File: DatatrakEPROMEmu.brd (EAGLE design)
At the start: 160 x 66 mm, 32 parts, among them IC1 LD1117AS33TR, IC2 XC95144XL_TQ144_P, U1 SN74LVCH16T245DGGR, U2 SN74LVCH16T245DGGR, U3 SN74LVCH16T245DGGR, U4 IS62WV25616DBLL-45TLI, U5 FT240XS, X1 MABC48B2, X2 PN61729-S

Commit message: first routable layout
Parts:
- added X3: (no value), con-molex:22-23-2061
- moved C9 35.3 mm to (119.4, 35.6), turned to 270 degrees
- moved C8 31.7 mm to (121.9, 35.6), turned to 270 degrees
- moved U5 23.3 mm to (128.3, 34.3), turned to 270 degrees
- moved R2 17.3 mm to (138.4, 27.9), turned to 180 degrees
- moved C7 15.3 mm to (143.5, 27.9), turned to 90 degrees
- moved R1 12.8 mm to (138.4, 31.8), turned to 180 degrees
- moved C19 10.3 mm to (48.3, 36.2)
- moved C20 10.3 mm to (67.3, 36.2)
- moved U4 10.3 mm to (57.8, 36.2)
- moved L1 9.25 mm to (138.4, 35.6), turned to 180 degrees
- moved C16 9.03 mm to (108.6, 33.0)
- moved C10 9.03 mm to (77.5, 46.4)
- moved C11 9.03 mm to (77.5, 41.3)
- moved C12 9.03 mm to (77.5, 31.1)
- moved C15 9.03 mm to (108.6, 25.4)
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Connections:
- removed net N$1: U3.1, U3.24
- new net /TGT_DEN: IC2.40, U3.25, U3.48
- new net A_LV18: IC2.53
- new net JTCK: IC2.67, X3.3
- new net JTDI: IC2.63, X3.1
- new net JTMS: IC2.65, X3.2
- new net TGT_DIR: IC2.41, U3.1, U3.24
- net +3V3: now also X3.5
- net /CE: now also U2.14; no longer U2.8
- net /CE_LV: now also IC2.43, U2.35; no longer U2.41
- net /OEH: now also U2.19; no longer U2.11
- net /OEH_LV: now also IC2.46, U2.30; no longer U2.38
- net /OEL: now also U2.17; no longer U2.9
- net /OEL_LV: now also IC2.45, U2.32; no longer U2.40
- net /PGMH: now also U1.20; no longer U2.6
- net /PGMH_LV: now also IC2.69, U1.29; no longer U2.43
- net /PGML: now also U1.23; no longer U2.5
- net /PGML_LV: now also IC2.71, U1.26; no longer U2.44
- net /RAM_CS: now also IC2.139
- net /RAM_LB: now also IC2.10
- net /RAM_OE: now also IC2.7
- net /RAM_UB: now also IC2.9
- net /RAM_WE: now also IC2.31
- net A0: now also U2.23; no longer U1.2
- net A1: now also U1.2; no longer U1.3
- net A10: now also U2.16; no longer U1.16
- net A11: now also U2.20; no longer U1.17
- net A12: now also U1.17; no longer U1.19
- net A13: now also U1.8; no longer U1.20
- net A14: now also U1.12; no longer U1.22
- net A15: now also U1.19; no longer U1.23
- net A16: now also U1.22; no longer U2.2
- net A17: now also U1.16; no longer U2.3
- net A4: now also U1.9; no longer U1.8
- net A5: now also U1.11; no longer U1.9
- net A6: now also U1.13; no longer U1.11
- net A7: now also U1.14; no longer U1.12
- net A8: now also U1.3; no longer U1.13
- net A9: now also U2.22; no longer U1.14
- net A_LV0: now also IC2.50, U2.26; no longer U1.47
- net A_LV1: now also IC2.51, U1.47; no longer U1.46
- net A_LV10: now also IC2.44, U2.33; no longer U1.33
- net A_LV11: now also IC2.48, U2.29; no longer U1.32
- net A_LV12: now also IC2.66, U1.32; no longer U1.30
- net A_LV13: now also IC2.56, U1.41; no longer U1.29
- net A_LV14: now also IC2.59, U1.37; no longer U1.27
- net A_LV15: now also IC2.68, U1.30; no longer U1.26
- net A_LV16: now also IC2.70, U1.27; no longer U2.47
- net A_LV17: now also IC2.64, U1.33; no longer U2.46
- net A_LV3: now also IC2.54
- net A_LV4: now also IC2.57, U1.40; no longer U1.41
- net A_LV5: now also IC2.58, U1.38; no longer U1.40
- net A_LV6: now also IC2.60, U1.36; no longer U1.38
- net A_LV7: now also IC2.61, U1.35; no longer U1.37
- net A_LV8: now also IC2.52, U1.46; no longer U1.36
- net A_LV9: now also IC2.49, U2.27; no longer U1.35
- net CLK24MHZ: now also IC2.38
- net D0: now also U3.23; no longer U3.2
- net D1: now also U3.22; no longer U3.3
- net D10: now also U3.8; no longer U3.16
- net D11: now also U3.2; no longer U3.17
- net D12: now also U3.3; no longer U3.19
- net D13: now also U3.5; no longer U3.20
- net D14: now also U3.6; no longer U3.22
- net D15: now also U3.11; no longer U3.23
- net D2: now also U3.20; no longer U3.5
- net D3: now also U3.19; no longer U3.6
- net D4: now also U3.17; no longer U3.8
- net D5: now also U3.16; no longer U3.9
- net D6: now also U3.14; no longer U3.11
- net D7: now also U3.13; no longer U3.12
- net D8: now also U3.12; no longer U3.13
- net D9: now also U3.9; no longer U3.14
- net D_LV0: now also IC2.32, U3.26, U4.16; no longer U3.47, U4.7
- net D_LV1: now also IC2.19, U3.27, U4.29; no longer U3.46, U4.8
- net D_LV10: now also IC2.13, U3.41, U4.36; no longer U3.33, U4.31
- net D_LV11: now also IC2.11, U3.47, U4.38; no longer U3.32, U4.32
- net D_LV12: now also IC2.138, U3.46, U4.7; no longer U3.30, U4.35
- net D_LV13: now also IC2.12, U3.44, U4.37; no longer U3.29, U4.36
- net D_LV14: now also IC2.137, U3.43, U4.8; no longer U3.27, U4.37
- net D_LV15: now also IC2.14, U3.38, U4.35; no longer U3.26, U4.38
- net D_LV2: now also IC2.33, U3.29, U4.15; no longer U3.44, U4.9
- net D_LV3: now also IC2.17, U3.30, U4.30; no longer U3.43, U4.10
- net D_LV4: now also IC2.34, U3.32, U4.14; no longer U3.41, U4.13
- net D_LV5: now also IC2.16, U3.33, U4.31; no longer U3.40, U4.14
- net D_LV6: now also IC2.35, U3.35, U4.13; no longer U3.38, U4.15
- net D_LV7: now also IC2.15, U3.36, U4.32; no longer U3.37, U4.16
- net D_LV8: now also U3.37, U4.10; no longer U3.36, U4.29
- net D_LV9: now also IC2.136, U3.40, U4.9; no longer U3.35, U4.30
- net FTDI_D0: now also IC2.105
- net FTDI_D1: now also IC2.102
- net FTDI_D2: now also IC2.103
- net FTDI_D3: now also IC2.97
- net FTDI_D4: now also IC2.104
- net FTDI_D5: now also IC2.100
- net FTDI_D6: now also IC2.98
- net FTDI_D7: now also IC2.101
- net FTDI_RD: now also IC2.96
- net FTDI_RXF: now also IC2.106
- net FTDI_TXE: now also IC2.107
- net FTDI_WR: now also IC2.95
- net GND: now also IC2.36, U1.1, U1.24, U2.11, U2.12, U2.13, U2.2, U2.5, U2.6, U2.8, U2.9, X3.6
- net JTDO: now also X3.4
- net RAMA0: now also IC2.140
- net RAMA1: now also IC2.142
- net RAMA10: now also IC2.22
- net RAMA11: now also IC2.23
- net RAMA12: now also IC2.25
- net RAMA13: now also IC2.26
- net RAMA14: now also IC2.27
- net RAMA15: now also IC2.28
- net RAMA16: now also IC2.30
- net RAMA17: now also IC2.24
- net RAMA2: now also IC2.143
- net RAMA3: now also IC2.2
- net RAMA4: now also IC2.3
- net RAMA5: now also IC2.4
- net RAMA6: now also IC2.5
- net RAMA7: now also IC2.6
- net RAMA8: now also IC2.20
- net RAMA9: now also IC2.21
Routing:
- net GND: track 96.6 -> 253.9 mm, vias 28 -> 50
- net +3V3: track 80.1 -> 115.6 mm, vias 12 -> 15
- net /TGT_DEN: track 0.00 -> 17.4 mm
- net TGT_DIR: track 0.00 -> 16.8 mm
- net +5V: track 13.4 -> 29.9 mm, vias 2 -> 7
- net N$7: track 14.3 -> 4.52 mm
- net N$3: track 8.79 -> 0.00 mm
- net N$6: track 8.58 -> 4.26 mm
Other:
- board size 160 x 66 mm -> 151.1 x 66 mm

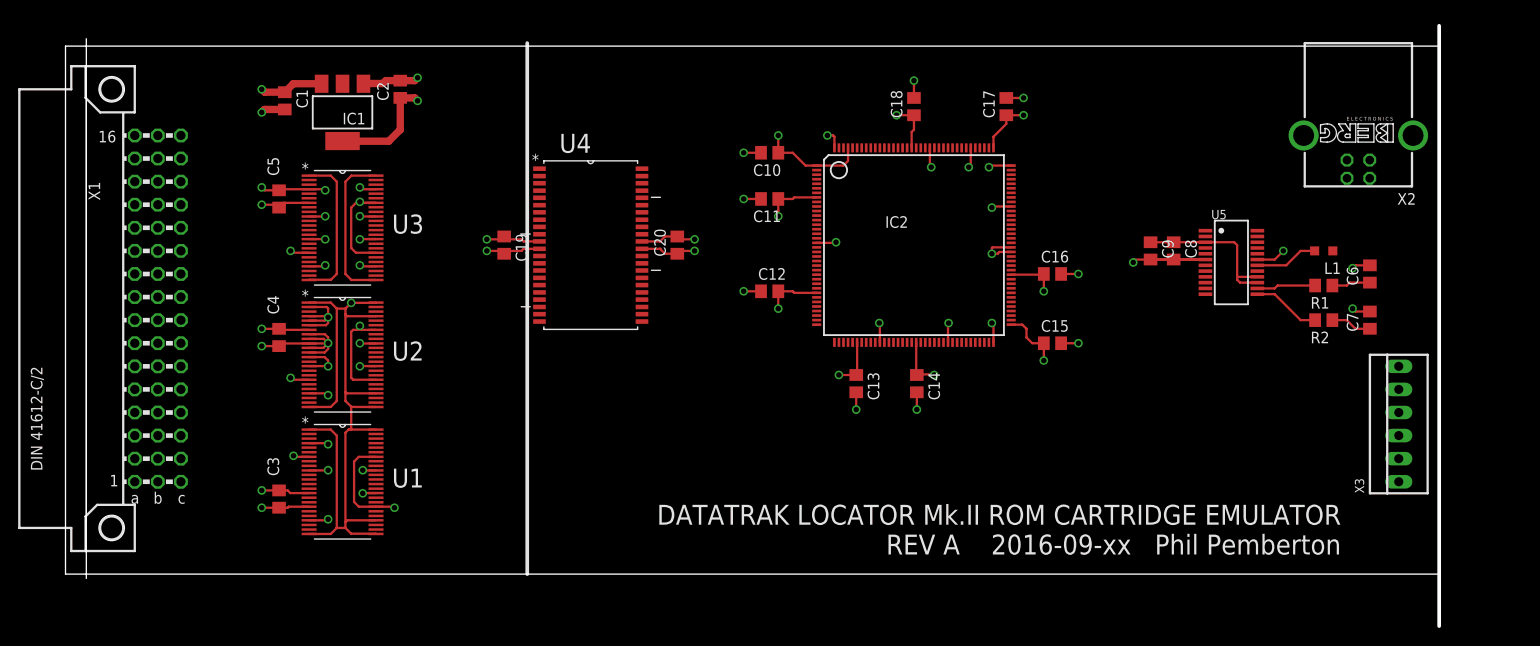
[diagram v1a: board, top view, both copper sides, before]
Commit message: add status LEDs
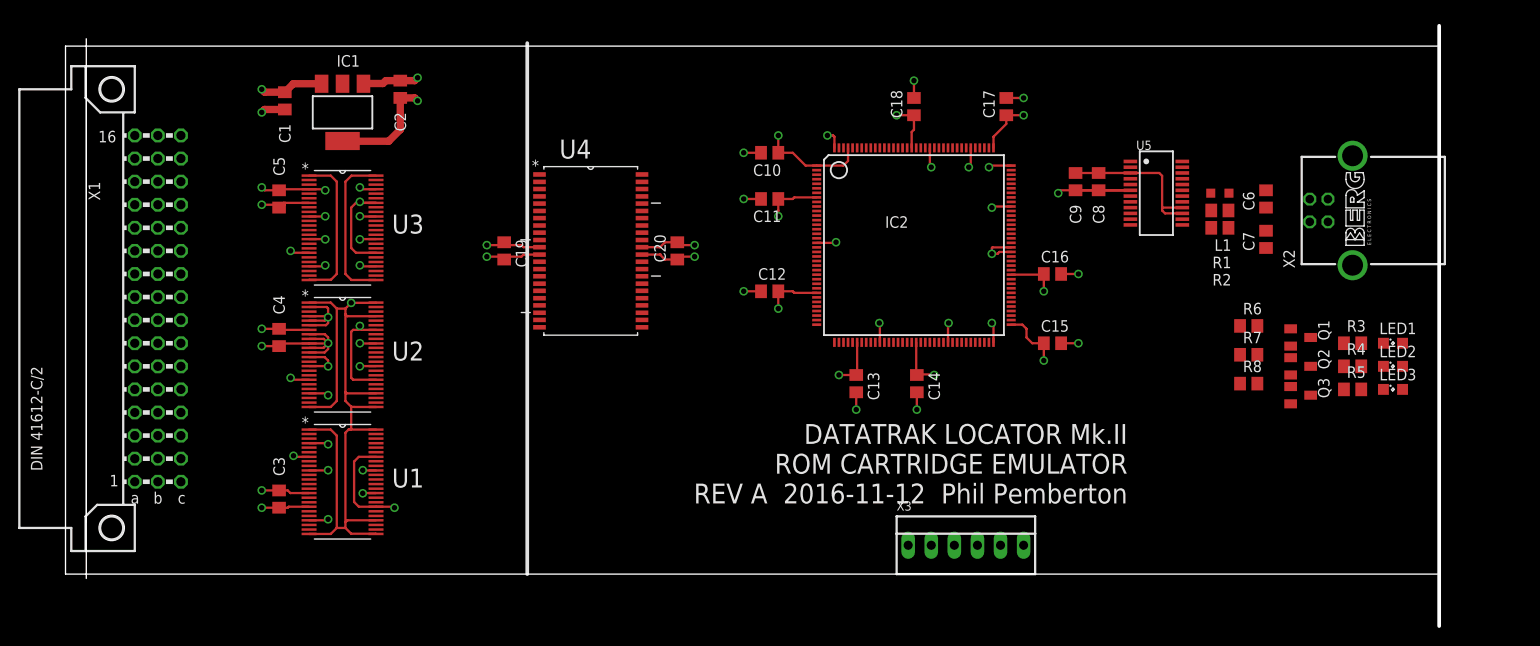
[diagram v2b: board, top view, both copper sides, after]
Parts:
- added LED1, LED2, LED3: (no value), led:SML0805
- added Q1, Q2, Q3: BC847CSMD, transistor-npn:SOT23
- added R3, R4, R5, R6, R7, R8: (no value), rcl:R0805
- moved X3 49.5 mm to (99.1, 3.17), turned to 0 degrees
- moved R2 15.3 mm to (127.0, 38.1)
- moved C7 14.5 mm to (132.1, 36.8), turned to 270 degrees
- moved R1 14.1 mm to (127.0, 40.0)
- moved C6 14.1 mm to (132.1, 41.3)
- moved L1 13.1 mm to (127.0, 41.9)
- moved U5 11.2 mm to (120.0, 41.9)
- moved C8 11.2 mm to (113.7, 43.2)
- moved C9 11.2 mm to (111.1, 43.2)
- moved X2 8.28 mm to (141.6, 40.0), turned to 90 degrees
- moved C19 0.63 mm to (48.3, 35.6)
- moved C20 0.63 mm to (67.3, 35.6)
- moved U4 0.63 mm to (57.8, 35.6)
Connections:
- new net N$1: Q1.3, R3.1
- new net N$10: Q3.3, R5.1
- new net N$11: LED1.C, R3.2
- new net N$12: LED2.C, R4.2
- new net N$13: LED3.C, R5.2
- new net N$16: IC2.82, R6.1
- new net N$17: IC2.81, R7.1
- new net N$18: IC2.80, R8.1
- new net N$19: Q1.1, R6.2
- new net N$20: Q2.1, R7.2
- new net N$21: Q3.1, R8.2
- new net N$9: Q2.3, R4.1
- net +3V3: now also LED1.A, LED2.A, LED3.A
- net GND: now also Q1.2, Q2.2, Q3.2
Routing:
- net N$5: track 7.54 -> 0.00 mm
- net GND: track 253.9 -> 246.5 mm, vias 50 -> 47
- net N$2: track 6.96 -> 0.00 mm
- net N$4: track 6.48 -> 0.00 mm
- net N$7: track 4.52 -> 0.00 mm
- net N$6: track 4.26 -> 0.00 mm
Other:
- board text added: "DATATRAK LOCATOR Mk.II ROM CARTRIDGE EMULATOR REV A 2016-11-12 Phil Pemberton"
- board text removed: "DATATRAK LOCATOR Mk.II ROM CARTRIDGE EMULATOR REV A 2016-09-xx Phil Pemberton"

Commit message: fully routed
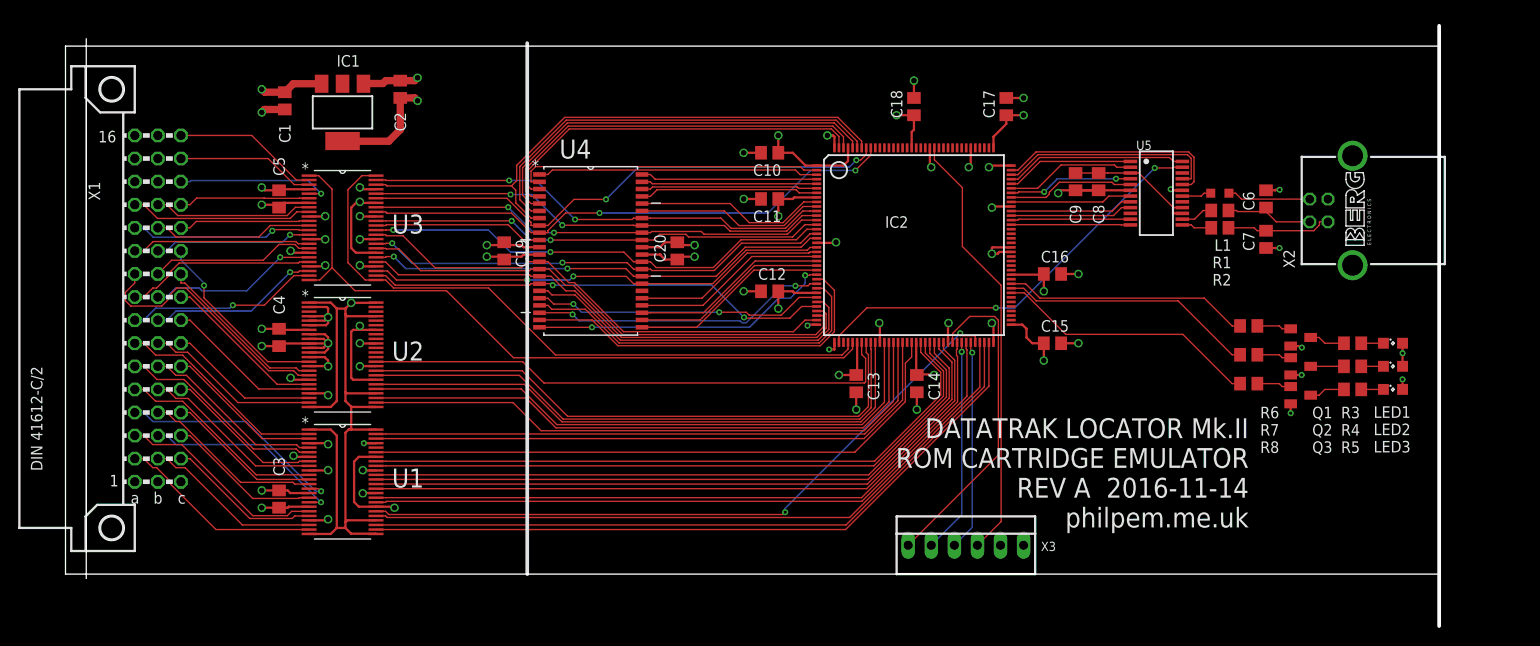
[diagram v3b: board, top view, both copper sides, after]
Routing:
- net /PGML_LV: track 0.00 -> 78.8 mm
- net A_LV16: track 0.00 -> 78.1 mm
- net /PGMH_LV: track 0.00 -> 77.4 mm
- net A_LV12: track 0.00 -> 75.8 mm
- net A_LV15: track 0.00 -> 75.4 mm, vias 0 -> 2
- net A_LV17: track 0.00 -> 75.0 mm
- net A_LV7: track 0.00 -> 74.6 mm
- net A_LV6: track 0.00 -> 74.1 mm
- net A_LV14: track 0.00 -> 73.6 mm
- net A_LV5: track 0.00 -> 73.1 mm
- net A_LV4: track 0.00 -> 72.4 mm
- net A_LV13: track 0.00 -> 71.8 mm
- net A_LV3: track 0.00 -> 67.4 mm
- net A_LV0: track 0.00 -> 66.0 mm
- net A_LV8: track 0.00 -> 66.0 mm
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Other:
- board text added: "DATATRAK LOCATOR Mk.II ROM CARTRIDGE EMULATOR REV A 2016-11-14 philpem.me.uk"
- board text removed: "DATATRAK LOCATOR Mk.II ROM CARTRIDGE EMULATOR REV A 2016-11-12 Phil Pemberton"

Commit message: added good-luck pangon to the silkscreen, this had better work
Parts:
- added U$1: (no value), chaoslogo:CHAOSLOGO
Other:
- board text added: "DATATRAK LOCATOR Mk.II ROM CARTRIDGE EMULATOR REV A 2016-11-14 PAP"
- board text removed: "DATATRAK LOCATOR Mk.II ROM CARTRIDGE EMULATOR REV A 2016-11-14 philpem.me.uk"
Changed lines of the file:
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@@
 <wire x1="50.8" y1="58.42" x2="50.8" y2="0" width="0.4064" layer="21"/>
 <wire x1="151.13" y1="60.325" x2="151.13" y2="-5.715" width="0.4064" layer="20"/>
-<text x="130.175" y="17.145" size="2.1844" layer="25" align="top-right">DATATRAK LOCATOR Mk.II
+<text x="123.825" y="16.51" size="2.1844" layer="25" align="top-right">DATATRAK LOCATOR Mk.II
 ROM CARTRIDGE EMULATOR
-REV A  2016-11-14
-philpem.me.uk</text>
+REV A  2016-11-14  PAP</text>
 </plain>
 <attributes>
@@
 <attribute name="VALUE" x="129.54" y="18.415" size="1.27" layer="27"/>
 </element>
+<element name="U$1" library="chaoslogo" package="CHAOSLOGO" value="" x="66.675" y="13.97"/>
 </elements>
 <signals>

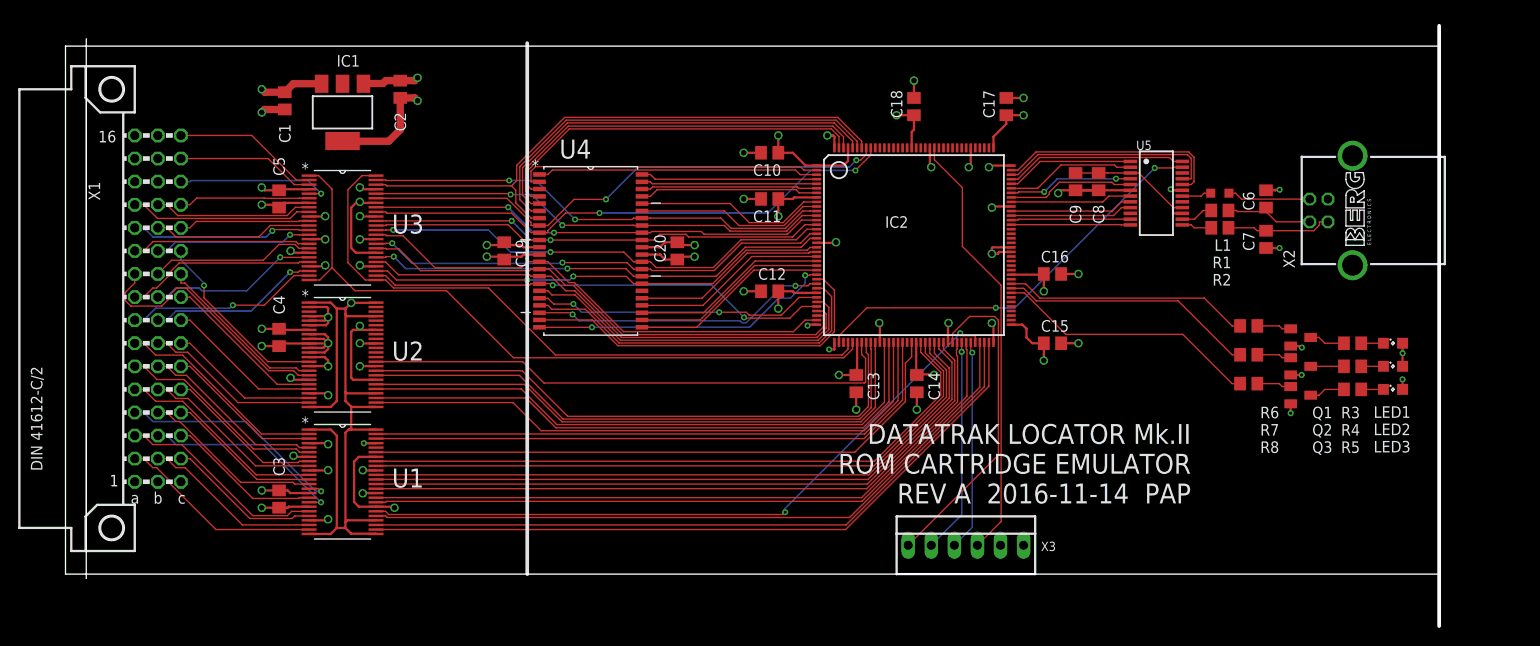
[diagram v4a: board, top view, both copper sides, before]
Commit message: fix a few missing routes and ERC errors
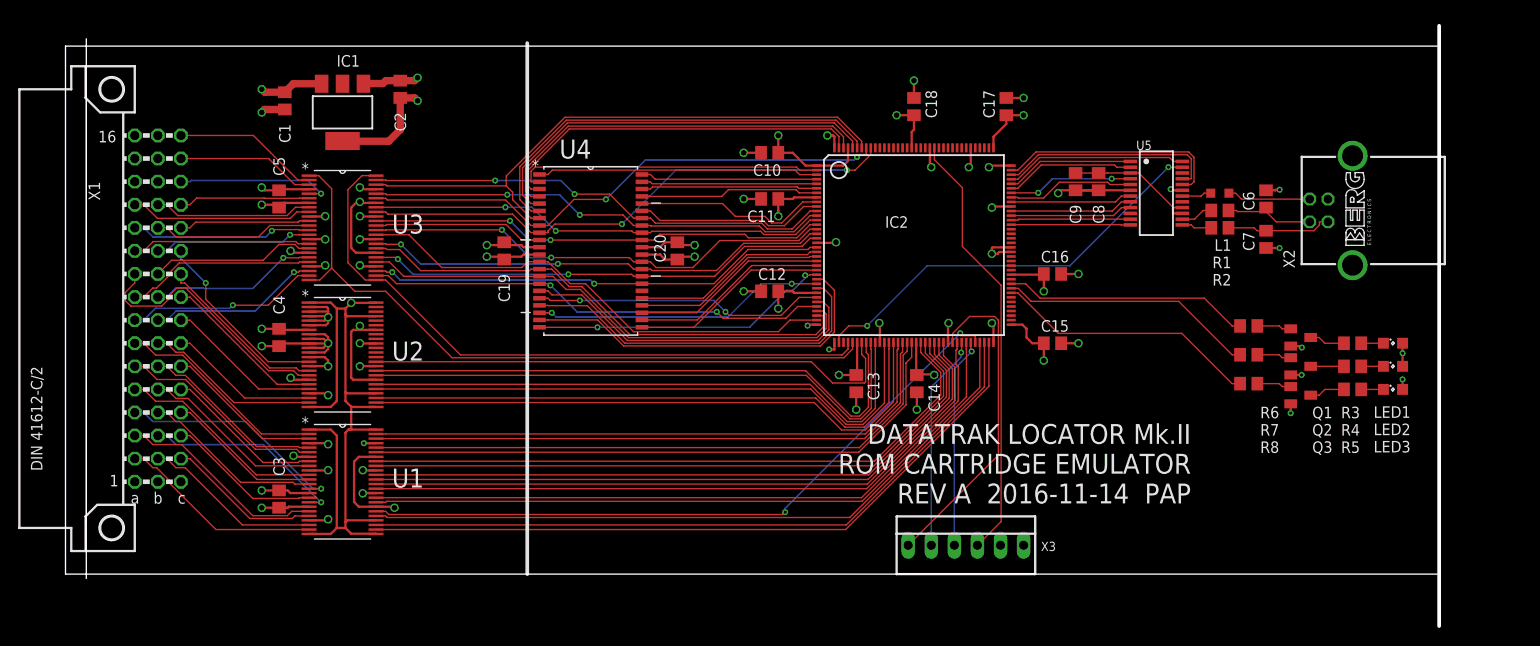
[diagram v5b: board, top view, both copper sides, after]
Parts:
- C10, C11, C12, C13, C14, C15, C16, C17, C18, C3, C4, C5: value (none) -> 100n
- LED1: value (none) -> RED
- LED2: value (none) -> YELLOW
- LED3: value (none) -> GREEN
- R6, R7, R8: value (none) -> 4k7
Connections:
- removed net A_LV18: IC2.53
- net A_LV2: now also IC2.53
- net GND: now also U2.3
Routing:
- net A_LV2: track 0.00 -> 66.9 mm
- net GND: track 244.1 -> 246.2 mm
- net RAMA14: track 32.7 -> 32.2 mm
